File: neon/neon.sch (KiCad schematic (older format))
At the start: 0 parts

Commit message: Add FT4232H module pinouts
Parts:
- added U?: FT4232H_CN3, symbol FTDI:FT4232H_CN3
- added U?: FT4232H_CN2, symbol FTDI:FT4232H_CN2
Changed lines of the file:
@@
 Comment4 ""
 $EndDescr
+$Comp
+L FTDI:FT4232H_CN3 U?
+U 1 1 5F4AA4CF
+P 4200 3300
+F 0 "U?" H 4825 3525 50  0000 C CNN
+F 1 "FT4232H_CN3" H 4825 3434 50  0000 C CNN
+F 2 "" H 5250 3400 50  0001 L CNN
+F 3 "" H 5250 3300 50  0001 L CNN
+	1    4200 3300
+	1    0    0    -1
+$EndComp
+$Comp
+L FTDI:FT4232H_CN2 U?
+U 1 1 5F4AB3F2
+P 6250 3300
+F 0 "U?" H 6875 3525 50  0000 C CNN
+F 1 "FT4232H_CN2" H 6875 3434 50  0000 C CNN
+F 2 "" H 7300 3400 50  0001 L CNN
+F 3 "" H 7300 3300 50  0001 L CNN
+	1    6250 3300
+	1    0    0    -1
+$EndComp
 $EndSCHEMATC

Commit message: Hierarchical version - draft
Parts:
- removed U?: FT4232H_CN3, symbol FTDI:FT4232H_CN3
- removed U?: FT4232H_CN2, symbol FTDI:FT4232H_CN2
- added U?: ABUS, symbol FTDI:ABUS
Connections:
- wire segments 0 -> 8
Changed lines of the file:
@@
 $Descr A4 11693 8268
 encoding utf-8
-Sheet 1 1
+Sheet 1 2
 Title "NEON - FT4232H Mini Module Adapter"
 Date "2020-08-29"
@@
 $EndDescr
 $Comp
-L FTDI:FT4232H_CN3 U?
-U 1 1 5F4AA4CF
-P 4200 3300
-F 0 "U?" H 4825 3525 50  0000 C CNN
-F 1 "FT4232H_CN3" H 4825 3434 50  0000 C CNN
-F 2 "" H 5250 3400 50  0001 L CNN
-F 3 "" H 5250 3300 50  0001 L CNN
-	1    4200 3300
+L FTDI:ABUS U?
+U 1 1 5F4C8005
+P 7500 3000
+F 0 "U?" H 7878 3001 50  0000 L CNN
+F 1 "ABUS" H 7878 2910 50  0000 L CNN
+F 2 "" H 7475 3675 50  0001 C CNN
+F 3 "" H 7475 3675 50  0001 C CNN
+	1    7500 3000
 	1    0    0    -1
 $EndComp
-$Comp
-L FTDI:FT4232H_CN2 U?
-U 1 1 5F4AB3F2
-P 6250 3300
-F 0 "U?" H 6875 3525 50  0000 C CNN
-F 1 "FT4232H_CN2" H 6875 3434 50  0000 C CNN
-F 2 "" H 7300 3400 50  0001 L CNN
-F 3 "" H 7300 3300 50  0001 L CNN
-	1    6250 3300
-	1    0    0    -1
-$EndComp
+$Sheet
+S 4450 2550 2350 2400
+U 5F4CB63F
+F0 "FT4232H.sch" 50
+F1 "FT4232H.sch" 50
+F2 "AD2" U R 6800 2900 50
+F3 "AD0" U R 6800 2700 50
+F4 "AD5" U R 6800 3200 50
+F5 "AD7" U R 6800 3400 50
+F6 "AD4" U R 6800 3100 50
+F7 "AD6" U R 6800 3300 50
+F8 "AD3" U R 6800 3000 50
+F9 "AD1" U R 6800 2800 50
+$EndSheet
+Wire Wire Line
+	6800 2900 7300 2900
+Wire Wire Line
+	6800 2700 7300 2700
+Wire Wire Line
+	6800 2800 7300 2800
+Wire Wire Line
+	7300 3000 6800 3000
+Wire Wire Line
+	6800 3100 7300 3100
+Wire Wire Line
+	6800 3200 7300 3200
+Wire Wire Line
+	6800 3300 7300 3300
+Wire Wire Line
+	7300 3400 6800 3400
 $EndSCHEMATC

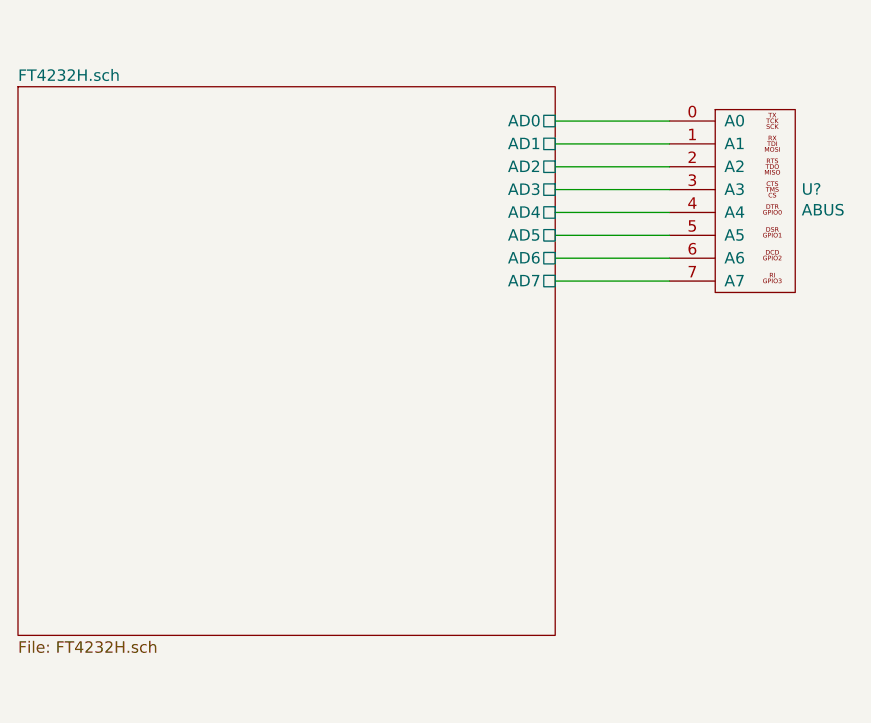
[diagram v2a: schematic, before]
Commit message: Add all hierarchical pins
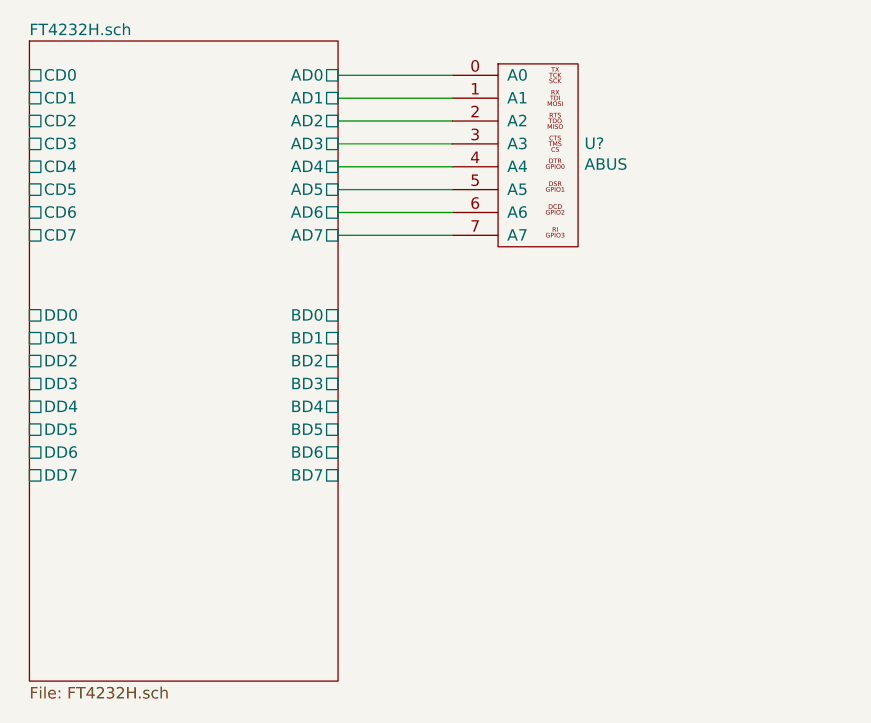
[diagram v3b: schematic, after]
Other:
- moved on the sheet: U?
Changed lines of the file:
@@
 L FTDI:ABUS U?
 U 1 1 5F4C8005
-P 7500 3000
-F 0 "U?" H 7878 3001 50  0000 L CNN
-F 1 "ABUS" H 7878 2910 50  0000 L CNN
-F 2 "" H 7475 3675 50  0001 C CNN
-F 3 "" H 7475 3675 50  0001 C CNN
-	1    7500 3000
+P 6550 2800
+F 0 "U?" H 6928 2801 50  0000 L CNN
+F 1 "ABUS" H 6928 2710 50  0000 L CNN
+F 2 "" H 6525 3475 50  0001 C CNN
+F 3 "" H 6525 3475 50  0001 C CNN
+	1    6550 2800
 	1    0    0    -1
 $EndComp
+Wire Wire Line
+	5850 2600 6350 2600
+Wire Wire Line
+	6350 2800 5850 2800
+Wire Wire Line
+	5850 3100 6350 3100
+Wire Wire Line
+	5850 2900 6350 2900
+Wire Wire Line
+	6350 3200 5850 3200
+Wire Wire Line
+	5850 3000 6350 3000
+Wire Wire Line
+	5850 2500 6350 2500
+Wire Wire Line
+	5850 2700 6350 2700
 $Sheet
-S 4450 2550 2350 2400
+S 4500 2350 1350 2800
 U 5F4CB63F
 F0 "FT4232H.sch" 50
 F1 "FT4232H.sch" 50
-F2 "AD2" U R 6800 2900 50
-F3 "AD0" U R 6800 2700 50
-F4 "AD5" U R 6800 3200 50
-F5 "AD7" U R 6800 3400 50
-F6 "AD4" U R 6800 3100 50
-F7 "AD6" U R 6800 3300 50
-F8 "AD3" U R 6800 3000 50
-F9 "AD1" U R 6800 2800 50
+F2 "AD2" U R 5850 2700 50
+F3 "AD0" U R 5850 2500 50
+F4 "AD5" U R 5850 3000 50
+F5 "AD7" U R 5850 3200 50
+F6 "AD4" U R 5850 2900 50
+F7 "AD6" U R 5850 3100 50
+F8 "AD3" U R 5850 2800 50
+F9 "AD1" U R 5850 2600 50
+F10 "BD0" U R 5850 3550 50
+F11 "BD2" U R 5850 3750 50
+F12 "BD4" U R 5850 3950 50
+F13 "BD5" U R 5850 4050 50
+F14 "BD7" U R 5850 4250 50
+F15 "BD1" U R 5850 3650 50
+F16 "BD3" U R 5850 3850 50
+F17 "BD6" U R 5850 4150 50
+F18 "DD7" U L 4500 4250 50
+F19 "DD5" U L 4500 4050 50
+F20 "DD4" U L 4500 3950 50
+F21 "DD2" U L 4500 3750 50
+F22 "DD0" U L 4500 3550 50
+F23 "CD6" U L 4500 3100 50
+F24 "CD4" U L 4500 2900 50
+F25 "CD3" U L 4500 2800 50
+F26 "CD1" U L 4500 2600 50
+F27 "CD0" U L 4500 2500 50
+F28 "CD2" U L 4500 2700 50
+F29 "CD5" U L 4500 3000 50
+F30 "CD7" U L 4500 3200 50
+F31 "DD1" U L 4500 3650 50
+F32 "DD3" U L 4500 3850 50
+F33 "DD6" U L 4500 4150 50
 $EndSheet
-Wire Wire Line
-	6800 2900 7300 2900
-Wire Wire Line
-	6800 2700 7300 2700
-Wire Wire Line
-	6800 2800 7300 2800
-Wire Wire Line
-	7300 3000 6800 3000
-Wire Wire Line
-	6800 3100 7300 3100
-Wire Wire Line
-	6800 3200 7300 3200
-Wire Wire Line
-	6800 3300 7300 3300
-Wire Wire Line
-	7300 3400 6800 3400
 $EndSCHEMATC

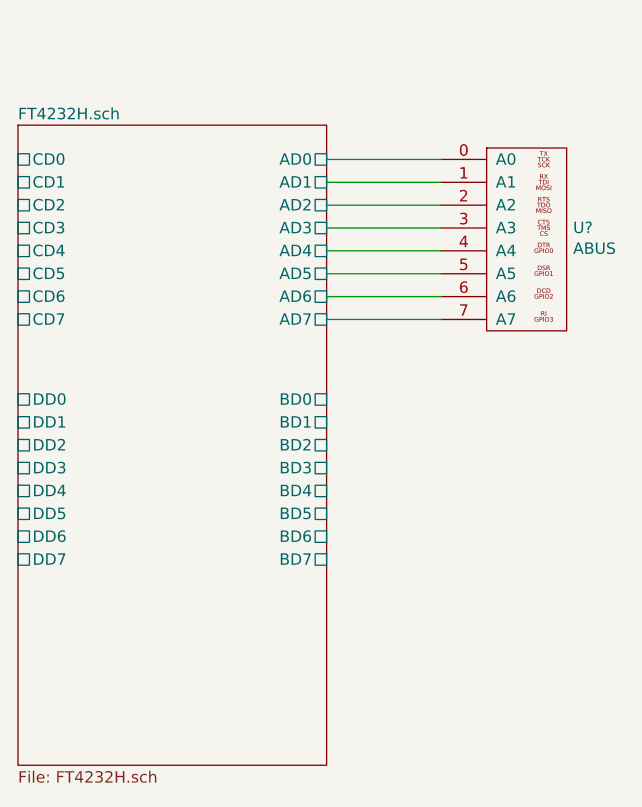
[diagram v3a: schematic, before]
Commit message: Add more hierarchical pins
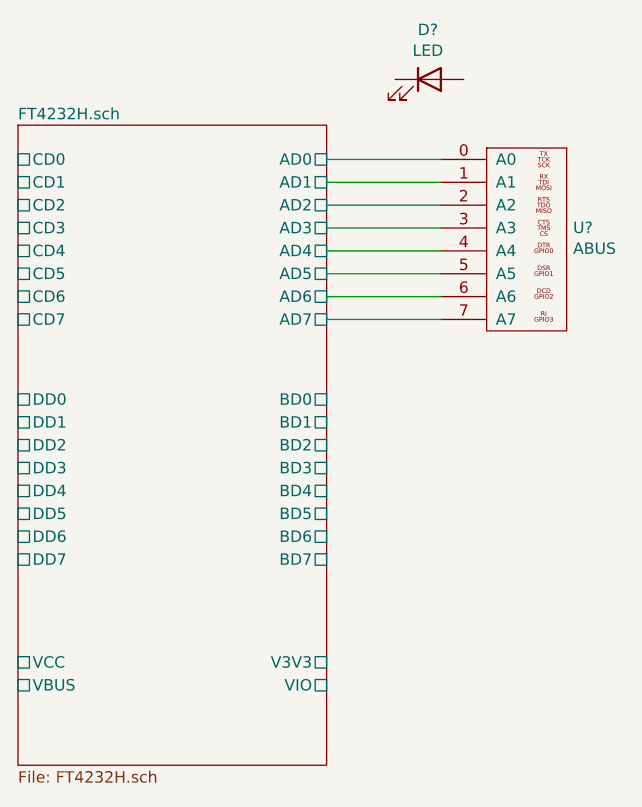
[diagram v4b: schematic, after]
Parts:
- added D?: LED, symbol Device:LED
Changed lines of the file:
@@
 Wire Wire Line
 	5850 2700 6350 2700
+$Comp
+L Device:LED D?
+U 1 1 5F4EB4AB
+P 6300 2150
+F 0 "D?" H 6293 2367 50  0000 C CNN
+F 1 "LED" H 6293 2276 50  0000 C CNN
+F 2 "" H 6300 2150 50  0001 C CNN
+F 3 "~" H 6300 2150 50  0001 C CNN
+	1    6300 2150
+	1    0    0    -1
+$EndComp
 $Sheet
 S 4500 2350 1350 2800
@@
 F32 "DD3" U L 4500 3850 50
 F33 "DD6" U L 4500 4150 50
+F34 "V3V3" U R 5850 4700 50
+F35 "VIO" U R 5850 4800 50
+F36 "VBUS" U L 4500 4800 50
+F37 "VCC" U L 4500 4700 50
 $EndSheet
 $EndSCHEMATC

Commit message: B, C & D buses
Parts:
- added J?: VBUS-VCC, symbol FTDI:VBUS-VCC
- added U?: BBUS, symbol FTDI:BBUS
- added U?: CBUS, symbol FTDI:CBUS
- added U?: DBUS, symbol FTDI:DBUS
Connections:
- net FT4232H.sch/BD0: now also U?.0 (B0)
- net FT4232H.sch/BD1: now also U?.1 (B1)
- net FT4232H.sch/BD2: now also U?.2 (B2)
- net FT4232H.sch/BD3: now also U?.3 (B3)
- net FT4232H.sch/BD4: now also U?.4 (B4)
- net FT4232H.sch/BD5: now also U?.5 (B5)
- net FT4232H.sch/BD6: now also U?.6 (B6)
- net FT4232H.sch/BD7: now also U?.7 (B7)
- net FT4232H.sch/CD0: now also U?.0 (C0)
- net FT4232H.sch/CD1: now also U?.1 (C1)
- net FT4232H.sch/CD2: now also U?.2 (C2)
- net FT4232H.sch/CD3: now also U?.3 (C3)
- net FT4232H.sch/CD4: now also U?.4 (C4)
- net FT4232H.sch/CD5: now also U?.5 (C5)
- net FT4232H.sch/CD6: now also U?.6 (C6)
- net FT4232H.sch/CD7: now also U?.7 (C7)
- net FT4232H.sch/DD0: now also U?.0 (D0)
- net FT4232H.sch/DD1: now also U?.1 (D1)
- net FT4232H.sch/DD2: now also U?.2 (D2)
- net FT4232H.sch/DD3: now also U?.3 (D3)
- net FT4232H.sch/DD4: now also U?.4 (D4)
- net FT4232H.sch/DD5: now also U?.5 (D5)
- net FT4232H.sch/DD6: now also U?.6 (D6)
- net FT4232H.sch/DD7: now also U?.7 (D7)
- net FT4232H.sch/VBUS: now also J?.1 (VCC)
- net FT4232H.sch/VCC: now also J?.0 (VBUS)
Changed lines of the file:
@@
 Comment4 ""
 $EndDescr
-$Comp
-L FTDI:ABUS U?
-U 1 1 5F4C8005
-P 6550 2800
-F 0 "U?" H 6928 2801 50  0000 L CNN
-F 1 "ABUS" H 6928 2710 50  0000 L CNN
-F 2 "" H 6525 3475 50  0001 C CNN
-F 3 "" H 6525 3475 50  0001 C CNN
-	1    6550 2800
-	1    0    0    -1
-$EndComp
 Wire Wire Line
 	5850 2600 6350 2600
@@
 Wire Wire Line
 	5850 2900 6350 2900
-Wire Wire Line
-	6350 3200 5850 3200
 Wire Wire Line
 	5850 3000 6350 3000
@@
 	1    0    0    -1
 $EndComp
+$Comp
+L FTDI:VBUS-VCC J?
+U 1 1 5F51B746
+P 3900 4700
+F 0 "J?" H 3800 4800 50  0000 L CNN
+F 1 "VBUS-VCC" H 4050 4500 50  0001 C CNN
+F 2 "" H 3900 4700 50  0001 C CNN
+F 3 "~" H 3900 4700 50  0001 C CNN
+	1    3900 4700
+	-1   0    0    -1
+$EndComp
+Wire Wire Line
+	4200 4700 4500 4700
+Wire Wire Line
+	4200 4800 4500 4800
+$Comp
+L FTDI:BBUS U?
+U 1 1 5F51EDE5
+P 6550 3850
+F 0 "U?" H 6928 3851 50  0000 L CNN
+F 1 "BBUS" H 6928 3760 50  0000 L CNN
+F 2 "" H 6525 4525 50  0001 C CNN
+F 3 "" H 6525 4525 50  0001 C CNN
+	1    6550 3850
+	1    0    0    -1
+$EndComp
+Wire Wire Line
+	6350 3550 5850 3550
+Wire Wire Line
+	5850 3650 6350 3650
+Wire Wire Line
+	6350 3750 5850 3750
+Wire Wire Line
+	5850 3850 6350 3850
+Wire Wire Line
+	6350 3950 5850 3950
+Wire Wire Line
+	5850 4050 6350 4050
+Wire Wire Line
+	6350 4150 5850 4150
+Wire Wire Line
+	5850 4250 6350 4250
+Wire Wire Line
+	4000 2600 4500 2600
+Wire Wire Line
+	4000 2800 4500 2800
+Wire Wire Line
+	4500 2700 4000 2700
+Wire Wire Line
+	6350 3200 5850 3200
+$Comp
+L FTDI:ABUS U?
+U 1 1 5F4C8005
+P 6550 2800
+F 0 "U?" H 6928 2801 50  0000 L CNN
+F 1 "ABUS" H 6928 2710 50  0000 L CNN
+F 2 "" H 6525 3475 50  0001 C CNN
+F 3 "" H 6525 3475 50  0001 C CNN
+	1    6550 2800
+	1    0    0    -1
+$EndComp
+$Comp
+L FTDI:CBUS U?
+U 1 1 5F520AE1
+P 3800 2800
+F 0 "U?" H 3867 3325 50  0000 C CNN
+F 1 "CBUS" H 3867 3234 50  0000 C CNN
+F 2 "" H 3775 3475 50  0001 C CNN
+F 3 "" H 3775 3475 50  0001 C CNN
+	1    3800 2800
+	-1   0    0    -1
+$EndComp
+Wire Wire Line
+	4500 2500 4000 2500
+Wire Wire Line
+	4000 2900 4500 2900
+Wire Wire Line
+	4500 3000 4000 3000
+Wire Wire Line
+	4000 3100 4500 3100
 $Sheet
 S 4500 2350 1350 2800
@@
 F32 "DD3" U L 4500 3850 50
 F33 "DD6" U L 4500 4150 50
-F34 "V3V3" U R 5850 4700 50
-F35 "VIO" U R 5850 4800 50
+F34 "V3V3" U R 5850 4800 50
+F35 "VIO" U R 5850 4700 50
 F36 "VBUS" U L 4500 4800 50
 F37 "VCC" U L 4500 4700 50
 $EndSheet
+Wire Wire Line
+	4000 3200 4500 3200
+$Comp
+L FTDI:DBUS U?
+U 1 1 5F52AE75
+P 3800 3850
+F 0 "U?" H 3867 4375 50  0000 C CNN
+F 1 "DBUS" H 3867 4284 50  0000 C CNN
+F 2 "" H 3775 4525 50  0001 C CNN
+F 3 "" H 3775 4525 50  0001 C CNN
+	1    3800 3850
+	-1   0    0    -1
+$EndComp
+Wire Wire Line
+	4000 3550 4500 3550
+Wire Wire Line
+	4500 3650 4000 3650
+Wire Wire Line
+	4000 3750 4500 3750
+Wire Wire Line
+	4500 3850 4000 3850
+Wire Wire Line
+	4000 3950 4500 3950
+Wire Wire Line
+	4500 4050 4000 4050
+Wire Wire Line
+	4000 4150 4500 4150
+Wire Wire Line
+	4500 4250 4000 4250
 $EndSCHEMATC

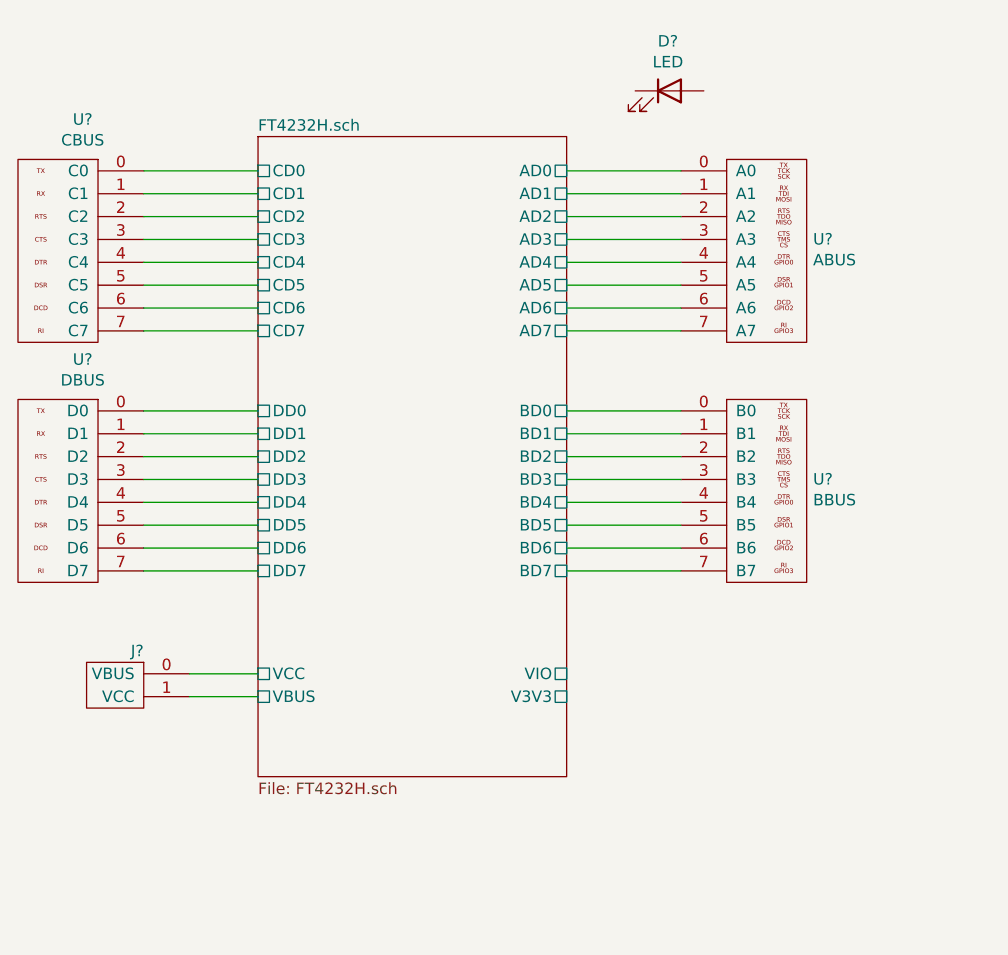
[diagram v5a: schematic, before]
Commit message: V3V3 & GND pings
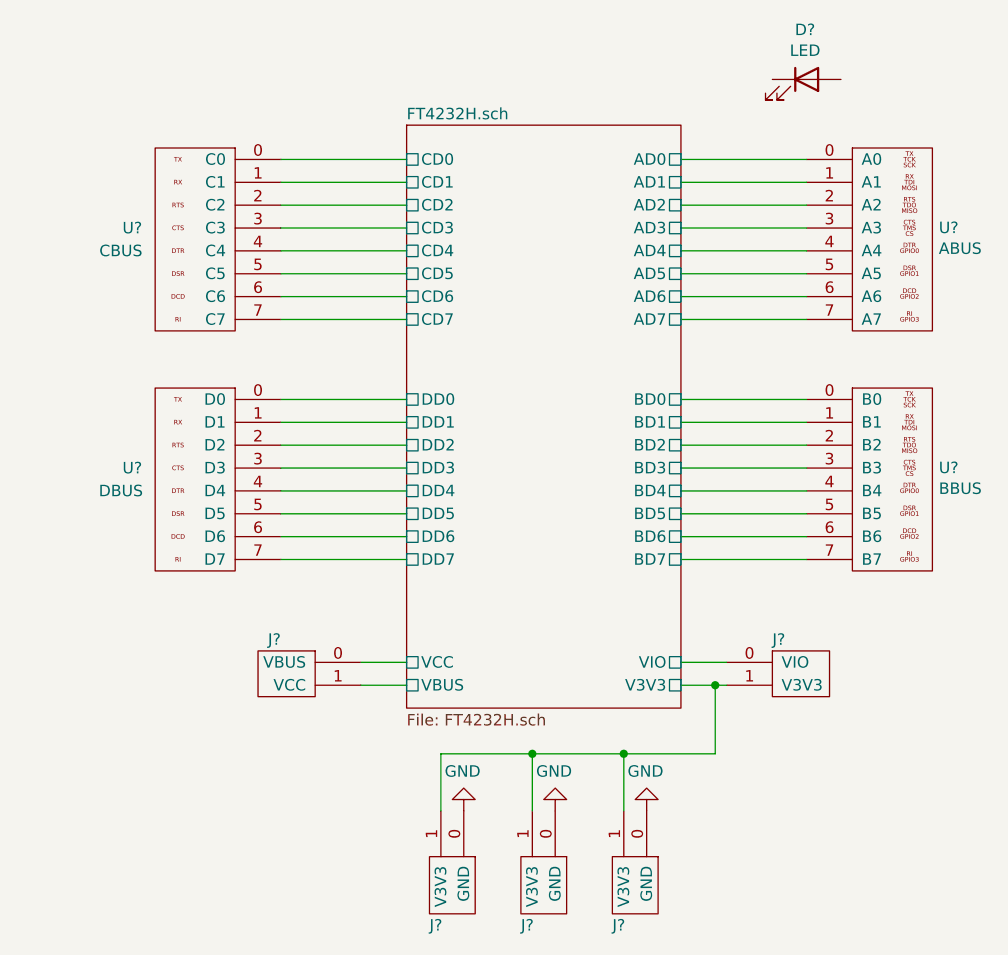
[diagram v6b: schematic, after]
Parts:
- added J?: V3V3-VIO, symbol FTDI:V3V3-VIO
- added J? (x3): V3V3-GND, symbol FTDI:V3V3-GND
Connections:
- net FT4232H.sch/V3V3: now also J?.1 (V3V3), J?.1 (V3V3), J?.1 (V3V3), J?.1 (V3V3)
- net FT4232H.sch/VIO: now also J?.0 (VIO)
- new net GND: J?.0 (GND), J?.0 (GND), J?.0 (GND)
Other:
- moved on the sheet: D?, J?, U?
